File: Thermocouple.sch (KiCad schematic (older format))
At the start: 15 parts

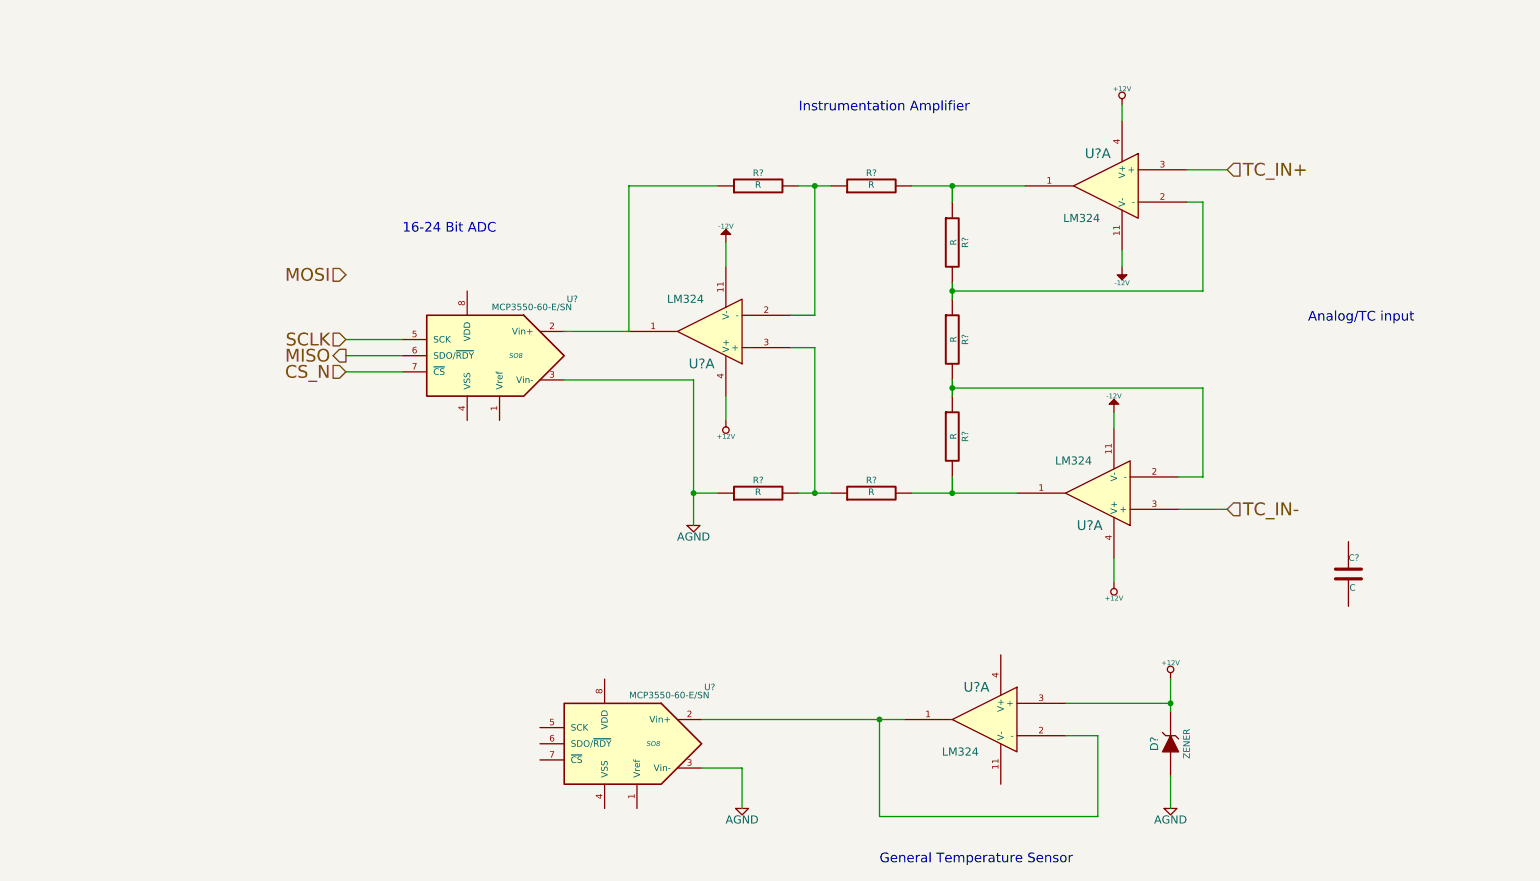
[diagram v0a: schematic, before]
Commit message: Added Relay module footprints.
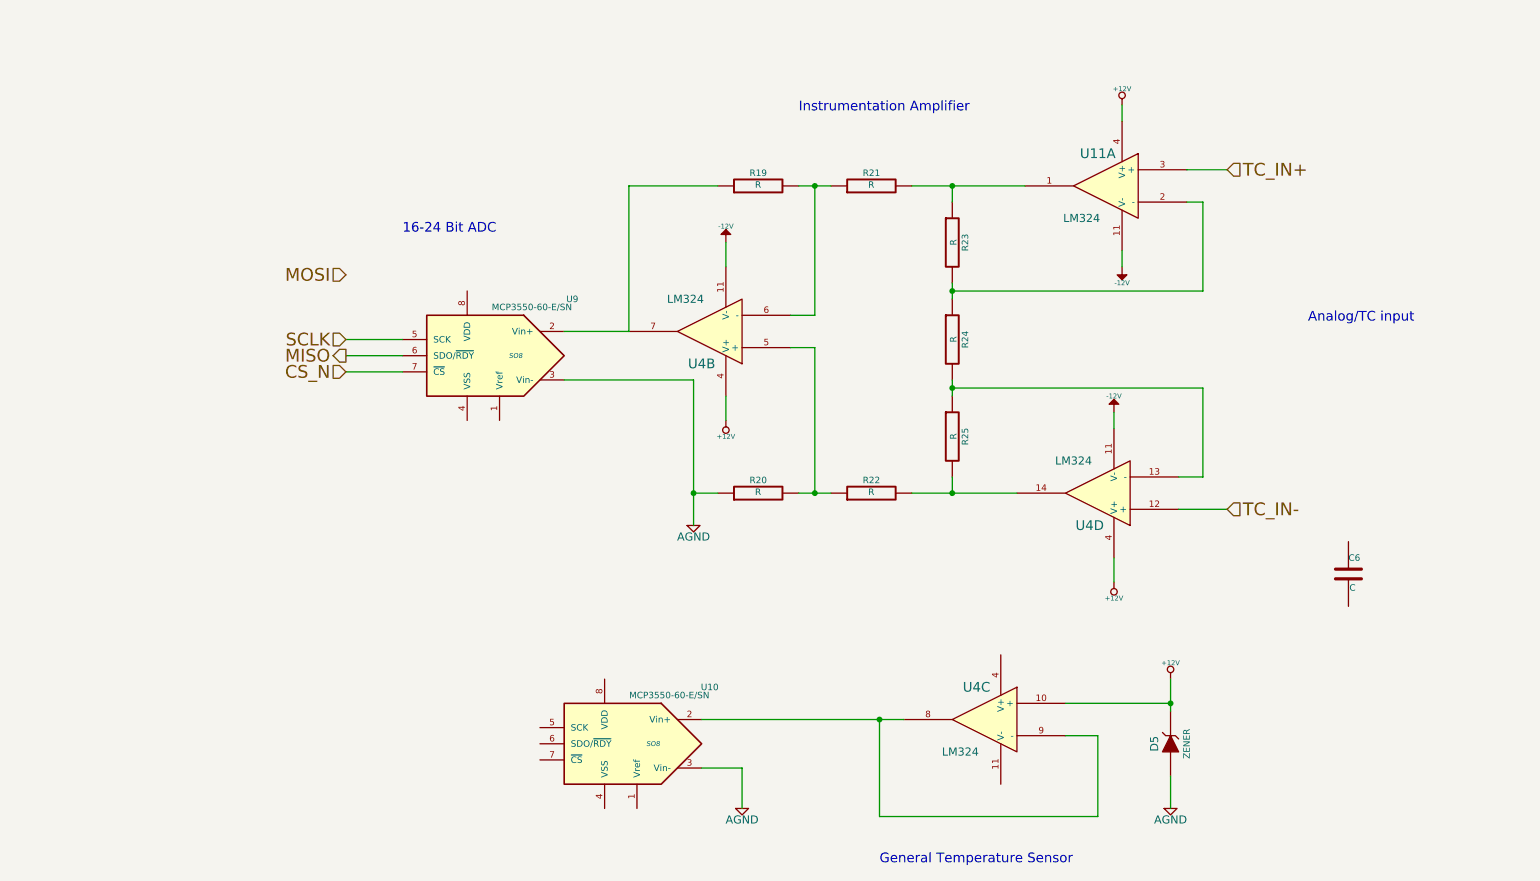
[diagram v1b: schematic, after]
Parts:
- gave numbers to parts that had none: 13
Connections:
- net +12V: now also U4.10 (+); no longer U4.3 (+)
- net TC_IN-: now also U4.12 (+); no longer U4.3 (+)
- net at R22.2, R25.2: now also U4.14; no longer U4.1
- net at R24.2, R25.1: now also U4.13 (-); no longer U4.2 (-)
- net at R19.1, U9.2 (Vin+): now also U4.7; no longer U4.1
- net at R19.2, R21.1: now also U4.6 (-); no longer U4.2 (-)
- net at R20.2, R22.1: now also U4.5 (+); no longer U4.3 (+)
- new net: U10.2 (Vin+), U4.8, U4.9 (-)
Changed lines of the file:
@@
 LIBS:valves
 LIBS:BB
+LIBS:GLSP
 LIBS:BB-cache
 EELAYER 24 0
@@
 CS_N
 $Comp
-L LM324 U?
+L LM324 U11
 U 1 1 52F42C35
 P 7350 1650
-F 0 "U?" H 7400 1850 60  0000 C CNN
+F 0 "U11" H 7400 1850 60  0000 C CNN
 F 1 "LM324" H 7500 1450 50  0000 C CNN
 F 2 "" H 7350 1650 60  0000 C CNN
@@
 $EndComp
 $Comp
-L LM324 U?
-U 1 1 52F42C56
+L LM324 U4
+U 4 1 52F42C56
 P 7300 3550
-F 0 "U?" H 7350 3750 60  0000 C CNN
+F 0 "U4" H 7350 3750 60  0000 C CNN
 F 1 "LM324" H 7450 3350 50  0000 C CNN
 F 2 "" H 7300 3550 60  0000 C CNN
 F 3 "" H 7300 3550 60  0000 C CNN
-	1    7300 3550
-	-1   0    0    1
-$EndComp
-$Comp
-L LM324 U?
-U 1 1 52F42C61
+	4    7300 3550
+	-1   0    0    1
+$EndComp
+$Comp
+L LM324 U4
+U 2 1 52F42C61
 P 4900 2550
-F 0 "U?" H 4950 2750 60  0000 C CNN
+F 0 "U4" H 4950 2750 60  0000 C CNN
 F 1 "LM324" H 5050 2350 50  0000 C CNN
 F 2 "" H 4900 2550 60  0000 C CNN
 F 3 "" H 4900 2550 60  0000 C CNN
-	1    4900 2550
-	-1   0    0    1
-$EndComp
-$Comp
-L LM324 U?
-U 1 1 52F42C6C
+	2    4900 2550
+	-1   0    0    1
+$EndComp
+$Comp
+L LM324 U4
+U 3 1 52F42C6C
 P 6600 4950
-F 0 "U?" H 6650 5150 60  0000 C CNN
+F 0 "U4" H 6650 5150 60  0000 C CNN
 F 1 "LM324" H 6750 4750 50  0000 C CNN
 F 2 "" H 6600 4950 60  0000 C CNN
 F 3 "" H 6600 4950 60  0000 C CNN
-	1    6600 4950
+	3    6600 4950
 	-1   0    0    -1
 $EndComp
 $Comp
-L R R?
+L R R23
 U 1 1 52F42C92
 P 6400 2000
-F 0 "R?" V 6480 2000 40  0000 C CNN
+F 0 "R23" V 6480 2000 40  0000 C CNN
 F 1 "R" V 6407 2001 40  0000 C CNN
 F 2 "" V 6330 2000 30  0000 C CNN
@@
 $EndComp
 $Comp
-L R R?
+L R R24
 U 1 1 52F42CA4
 P 6400 2600
-F 0 "R?" V 6480 2600 40  0000 C CNN
+F 0 "R24" V 6480 2600 40  0000 C CNN
 F 1 "R" V 6407 2601 40  0000 C CNN
 F 2 "" V 6330 2600 30  0000 C CNN
@@
 $EndComp
 $Comp
-L R R?
+L R R25
 U 1 1 52F42CAF
 P 6400 3200
-F 0 "R?" V 6480 3200 40  0000 C CNN
+F 0 "R25" V 6480 3200 40  0000 C CNN
 F 1 "R" V 6407 3201 40  0000 C CNN
 F 2 "" V 6330 3200 30  0000 C CNN
@@
 	6150 3550 6800 3550
 $Comp
-L C C?
+L C C6
 U 1 1 52F42D15
 P 8850 4050
-F 0 "C?" H 8850 4150 40  0000 L CNN
+F 0 "C6" H 8850 4150 40  0000 L CNN
 F 1 "C" H 8856 3965 40  0000 L CNN
 F 2 "" H 8888 3900 30  0000 C CNN
@@
 $EndComp
 $Comp
-L R R?
+L R R21
 U 1 1 52F42D44
 P 5900 1650
-F 0 "R?" V 5980 1650 40  0000 C CNN
+F 0 "R21" V 5980 1650 40  0000 C CNN
 F 1 "R" V 5907 1651 40  0000 C CNN
 F 2 "" V 5830 1650 30  0000 C CNN
@@
 $EndComp
 $Comp
-L R R?
+L R R22
 U 1 1 52F42D4F
 P 5900 3550
-F 0 "R?" V 5980 3550 40  0000 C CNN
+F 0 "R22" V 5980 3550 40  0000 C CNN
 F 1 "R" V 5907 3551 40  0000 C CNN
 F 2 "" V 5830 3550 30  0000 C CNN
@@
 $EndComp
 $Comp
-L R R?
+L R R20
 U 1 1 52F42D5A
 P 5200 3550
-F 0 "R?" V 5280 3550 40  0000 C CNN
+F 0 "R20" V 5280 3550 40  0000 C CNN
 F 1 "R" V 5207 3551 40  0000 C CNN
 F 2 "" V 5130 3550 30  0000 C CNN
@@
 $EndComp
 $Comp
-L R R?
+L R R19
 U 1 1 52F42D65
 P 5200 1650
-F 0 "R?" V 5280 1650 40  0000 C CNN
+F 0 "R19" V 5280 1650 40  0000 C CNN
 F 1 "R" V 5207 1651 40  0000 C CNN
 F 2 "" V 5130 1650 30  0000 C CNN
@@
 	8100 3650 7800 3650
 $Comp
-L +12V #PWR?
+L +12V #PWR47
 U 1 1 52F42F10
 P 7400 4100
-F 0 "#PWR?" H 7400 4050 20  0001 C CNN
+F 0 "#PWR47" H 7400 4050 20  0001 C CNN
 F 1 "+12V" H 7400 4200 30  0000 C CNN
 F 2 "" H 7400 4100 60  0000 C CNN
@@
 $EndComp
 $Comp
-L -12V #PWR?
+L -12V #PWR49
 U 1 1 52F42F24
 P 7450 2150
-F 0 "#PWR?" H 7450 2280 20  0001 C CNN
+F 0 "#PWR49" H 7450 2280 20  0001 C CNN
 F 1 "-12V" H 7450 2250 30  0000 C CNN
 F 2 "" H 7450 2150 60  0000 C CNN
@@
 $EndComp
 $Comp
-L +12V #PWR?
+L +12V #PWR48
 U 1 1 52F42F40
 P 7450 1150
-F 0 "#PWR?" H 7450 1100 20  0001 C CNN
+F 0 "#PWR48" H 7450 1100 20  0001 C CNN
 F 1 "+12V" H 7450 1250 30  0000 C CNN
 F 2 "" H 7450 1150 60  0000 C CNN
@@
 $EndComp
 $Comp
-L -12V #PWR?
+L -12V #PWR46
 U 1 1 52F42F4B
 P 7400 3050
-F 0 "#PWR?" H 7400 3180 20  0001 C CNN
+F 0 "#PWR46" H 7400 3180 20  0001 C CNN
 F 1 "-12V" H 7400 3150 30  0000 C CNN
 F 2 "" H 7400 3050 60  0000 C CNN
@@
 $EndComp
 $Comp
-L -12V #PWR?
+L -12V #PWR43
 U 1 1 52F42F56
 P 5000 2000
-F 0 "#PWR?" H 5000 2130 20  0001 C CNN
+F 0 "#PWR43" H 5000 2130 20  0001 C CNN
 F 1 "-12V" H 5000 2100 30  0000 C CNN
 F 2 "" H 5000 2000 60  0000 C CNN
@@
 $EndComp
 $Comp
-L +12V #PWR?
+L +12V #PWR44
 U 1 1 52F42F61
 P 5000 3100
-F 0 "#PWR?" H 5000 3050 20  0001 C CNN
+F 0 "#PWR44" H 5000 3050 20  0001 C CNN
 F 1 "+12V" H 5000 3200 30  0000 C CNN
 F 2 "" H 5000 3100 60  0000 C CNN
@@
 	7450 1250 7450 1150
 $Comp
-L AGND #PWR?
+L AGND #PWR42
 U 1 1 52F4308B
 P 4800 3750
-F 0 "#PWR?" H 4800 3750 40  0001 C CNN
+F 0 "#PWR42" H 4800 3750 40  0001 C CNN
 F 1 "AGND" H 4800 3680 50  0000 C CNN
 F 2 "" H 4800 3750 60  0000 C CNN
@@
 	4800 2850 4800 3750
 $Comp
-L MCP3550-60-E/SN U?
+L MCP3550-60-E/SN U9
 U 1 1 52F430CA
 P 3500 2700
-F 0 "U?" H 2950 3050 40  0000 C CNN
+F 0 "U9" H 2950 3050 40  0000 C CNN
 F 1 "MCP3550-60-E/SN" H 3200 3000 40  0000 C CNN
 F 2 "SO8" H 3300 2700 30  0000 C CIN
@@
 	3000 2800 2650 2800
 $Comp
-L MCP3550-60-E/SN U?
+L MCP3550-60-E/SN U10
 U 1 1 52F431D7
 P 4350 5100
-F 0 "U?" H 3800 5450 40  0000 C CNN
+F 0 "U10" H 3800 5450 40  0000 C CNN
 F 1 "MCP3550-60-E/SN" H 4050 5400 40  0000 C CNN
 F 2 "SO8" H 4150 5100 30  0000 C CIN
@@
 Connection ~ 4800 3550
 $Comp
-L ZENER D?
+L ZENER D5
 U 1 1 52F43290
 P 7750 5100
-F 0 "D?" H 7750 5200 50  0000 C CNN
+F 0 "D5" H 7750 5200 50  0000 C CNN
 F 1 "ZENER" H 7750 5000 40  0000 C CNN
 F 2 "" H 7750 5100 60  0000 C CNN
@@
 	7750 4700 7750 4900
 $Comp
-L +12V #PWR?
+L +12V #PWR50
 U 1 1 52F432EC
 P 7750 4700
-F 0 "#PWR?" H 7750 4650 20  0001 C CNN
+F 0 "#PWR50" H 7750 4650 20  0001 C CNN
 F 1 "+12V" H 7750 4800 30  0000 C CNN
 F 2 "" H 7750 4700 60  0000 C CNN
@@
 Connection ~ 7750 4850
 $Comp
-L AGND #PWR?
+L AGND #PWR51
 U 1 1 52F43328
 P 7750 5500
-F 0 "#PWR?" H 7750 5500 40  0001 C CNN
+F 0 "#PWR51" H 7750 5500 40  0001 C CNN
 F 1 "AGND" H 7750 5430 50  0000 C CNN
 F 2 "" H 7750 5500 60  0000 C CNN
@@
 Connection ~ 5950 4950
 $Comp
-L AGND #PWR?
+L AGND #PWR45
 U 1 1 52F4345C
 P 5100 5500
-F 0 "#PWR?" H 5100 5500 40  0001 C CNN
+F 0 "#PWR45" H 5100 5500 40  0001 C CNN
 F 1 "AGND" H 5100 5430 50  0000 C CNN
 F 2 "" H 5100 5500 60  0000 C CNN

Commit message: Associated and placed thermocouple, terminal, arduino, fan driver, power protection modules.
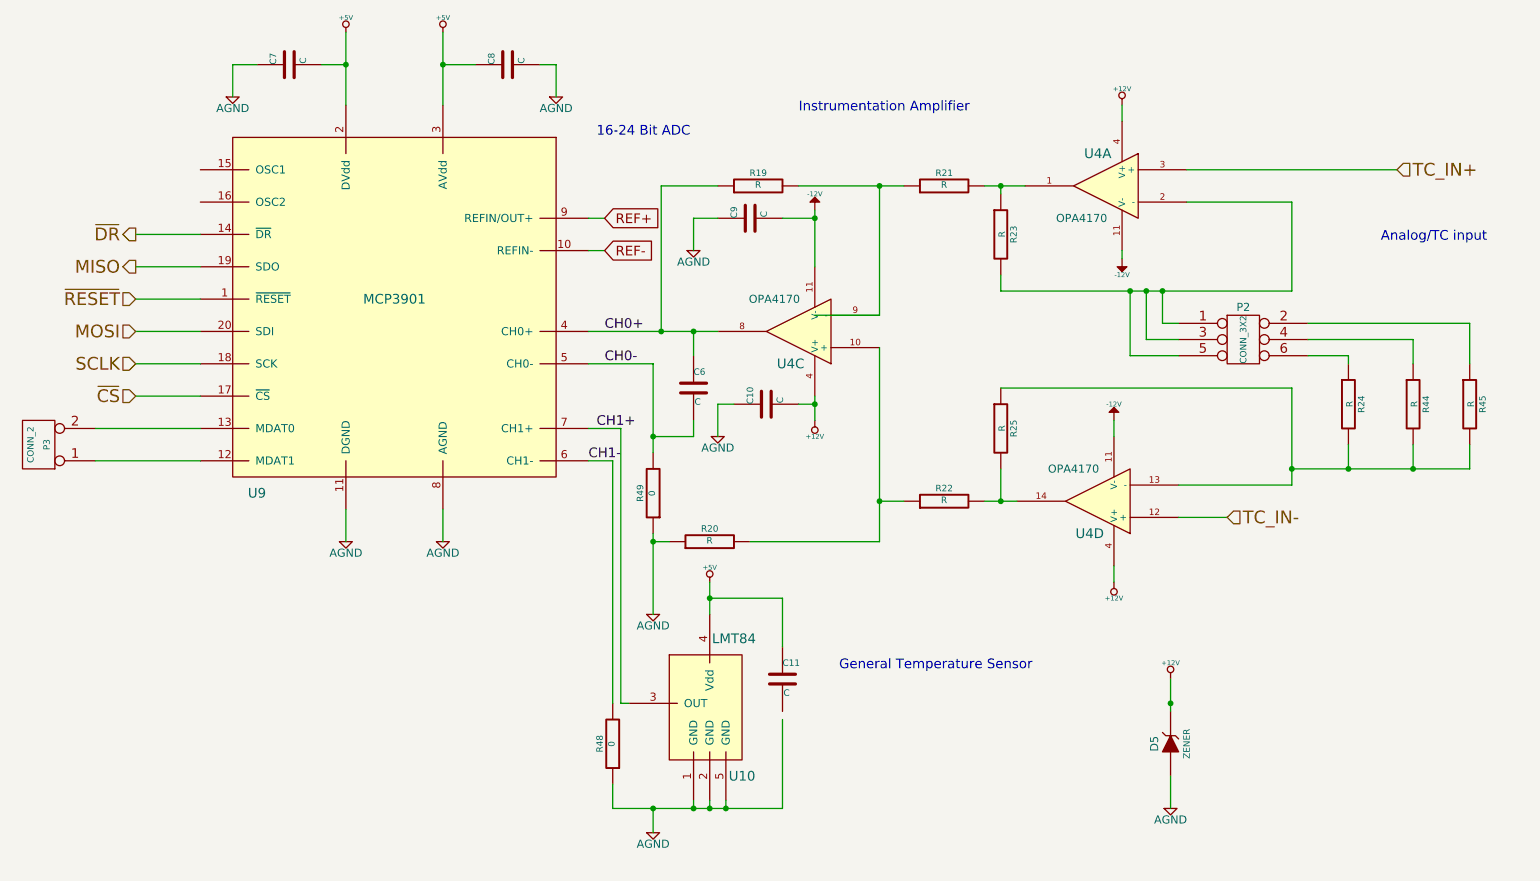
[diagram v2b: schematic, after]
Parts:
- removed U10, U9: MCP3550-60-E/SN, SO8, symbol MCP3550-60-E/SN
- removed unit 3 of U4
- added C10, C11, C7, C8, C9: C, symbol C
- added P2: CONN_3X2, symbol CONN_3X2
- added P3: CONN_2, symbol CONN_2
- added R44, R45: R, symbol R
- added R48, R49: 0, symbol R
- added U10: LMT84, symbol LMT84
- added U9: MCP3901, symbol MCP3901
- U4: renamed from U11; value LM324 -> OPA4170
- U4: value LM324 -> OPA4170
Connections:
- net +12V: now also C10.2
- net -12V: now also C9.2
- net AGND: now also C10.1, C7.1, C8.2, C9.1, R48.1, R49.1, U10.1 (GND), U10.2 (GND), U10.5 (GND), U9.11 (DGND), U9.8 (AGND)
- net MISO: now also U9.19 (SDO)
- net MOSI: now also U9.20 (SDI)
- net SCLK: now also U9.18 (SCK)
- net at R23.2, U4.2 (-): now also P2.1, P2.3, P2.5; no longer R24.1
- net at R24.2, R25.1, U4.13 (-): now also R44.2, R45.2
- net at R20.2, R22.1: now also U4.10 (+); no longer U4.5 (+)
- net at R19.2, R21.1: now also U4.9 (-); no longer U4.6 (-)
- net CH0+: now reaches R19.1
- net CH0+: now also C6.1, U4.8, U9.4 (CH0+); no longer U4.7
- net CH0-: now reaches C6.2
- net CH0-: now also R49.2, U9.5 (CH0-)
- new net: P2.6, R24.1
- new net: P3.1 (P1), U9.12 (MDAT1)
- new net: P3.2 (PM), U9.13 (MDAT0)
- new net: P2.4, R44.1
- new net: P2.2, R45.1
- new net +5V: C11.1, C7.2, C8.1, U10.4 (Vdd), U9.2 (DVdd), U9.3 (AVdd)
- new net CH1+: U10.3 (OUT), U9.7 (CH1+)
- new net CH1-: R48.2, U9.6 (CH1-)
- new net REF+: U9.9 (REFIN/OUT+)
- new net REF-: U9.10 (REFIN-)
- new net ~CS: U9.17 (~CS)
- new net ~DR: U9.14 (~DR)
- new net ~RESET: U9.1 (~RESET)
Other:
- moved on the sheet: C6, R20, R21, R22, R23, R24, R25, U4D

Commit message: Layout sessions 1-4.
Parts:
- removed D5: ZENER, symbol ZENER
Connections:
- net AGND: now also C11.2
- net +12V renamed FE_V+
- net -12V renamed FE_V-
